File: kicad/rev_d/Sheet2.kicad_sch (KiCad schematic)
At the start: 181 parts, among them J10 vg_old, J5 external clock, J6 JUMPER, J8 JUMPER, J9 JUMPER, Q2 QUARTZ, Q3 QUARTZ32768, U2 PCA9555DB, X11 KEYB-MOUSE, X12 IDC20, X13 USB_C, X15 PLB2-2, X19 AVR pgm conn, X3 IDC26LPT, X4 IDC10M, X5 IDC10M, X6 RS232_9

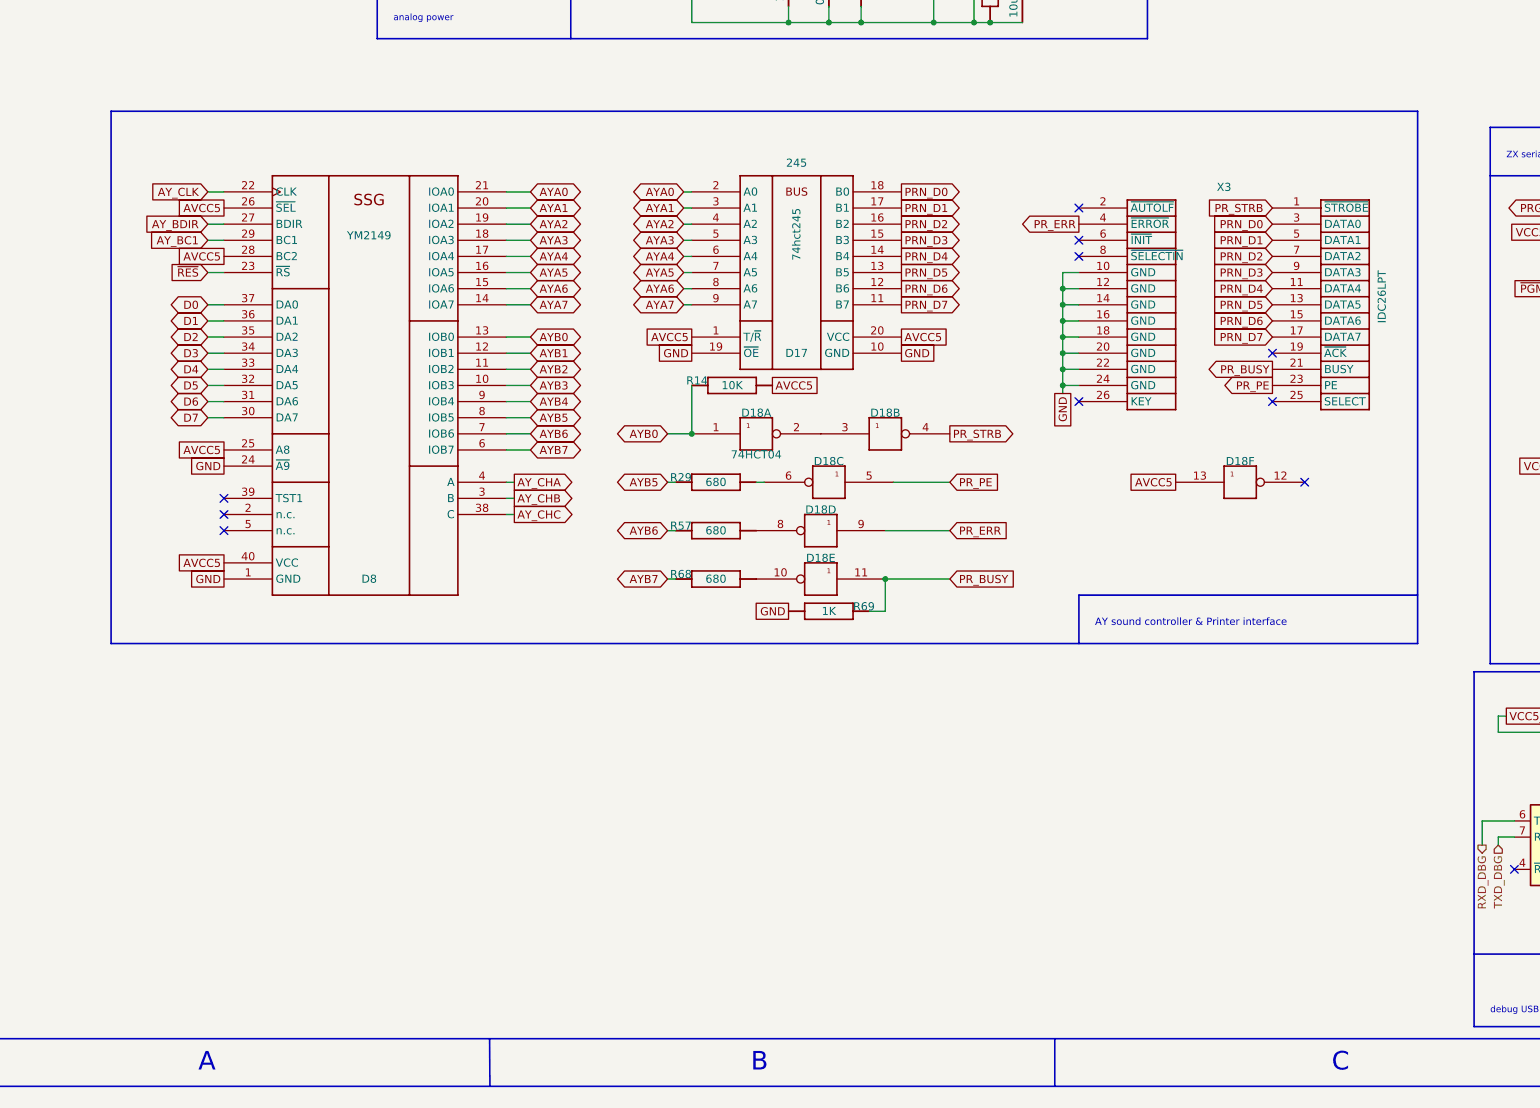
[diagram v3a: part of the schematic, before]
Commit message: pentevo: rev D: add turbosound connector parallel to AY
git-svn-id: svn://localhost/local-pentevo@1264 c6c76956-fad2-4150-a3a9-ea0a427205ba
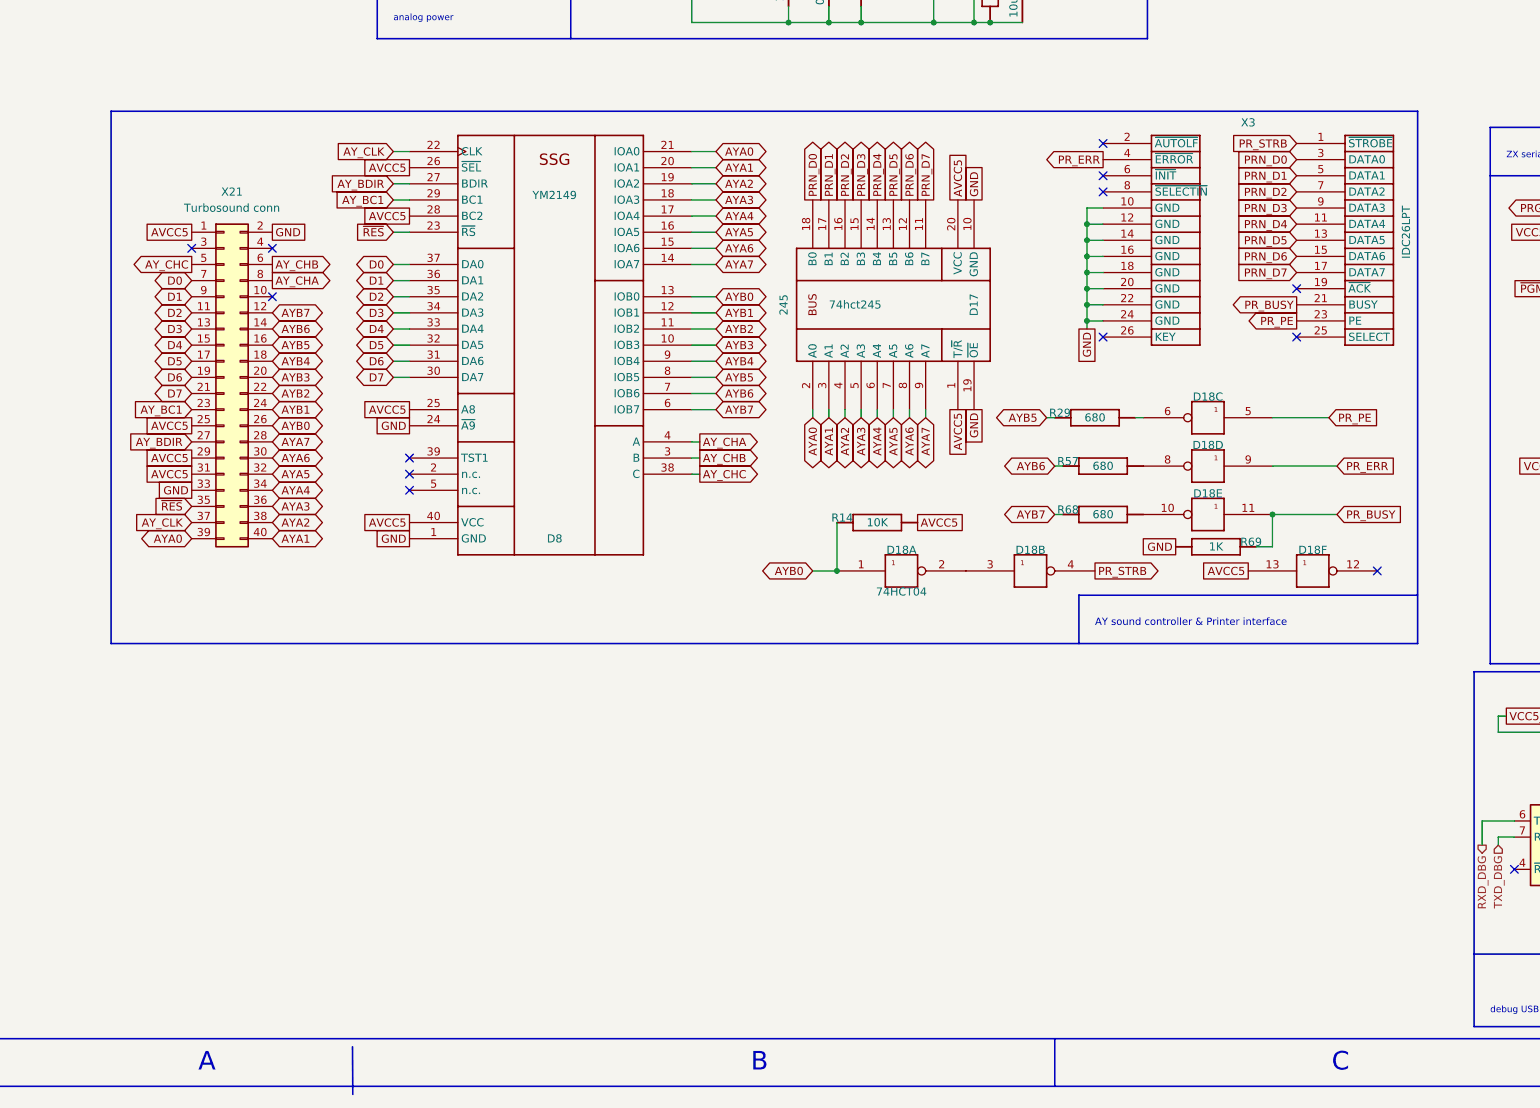
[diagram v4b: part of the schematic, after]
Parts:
- added X21: Turbosound conn, Connector_IDC:IDC-Header_2x20_P2.54mm_Vertical, symbol Connector_Generic:Conn_02x20_Odd_Even
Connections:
- net AVCC5: now also X21.1 (Pin_1), X21.25 (Pin_25), X21.29 (Pin_29), X21.31 (Pin_31)
- net AYA0: now also X21.39 (Pin_39)
- net AYA1: now also X21.40 (Pin_40)
- net AYA2: now also X21.38 (Pin_38)
- net AYA3: now also X21.36 (Pin_36)
- net AYA4: now also X21.34 (Pin_34)
- net AYA5: now also X21.32 (Pin_32)
- net AYA6: now also X21.30 (Pin_30)
- net AYA7: now also X21.28 (Pin_28)
- net AYB0: now also X21.26 (Pin_26)
- net AYB1: now also X21.24 (Pin_24)
- net AYB2: now also X21.22 (Pin_22)
- net AYB3: now also X21.20 (Pin_20)
- net AYB4: now also X21.18 (Pin_18)
- net AYB5: now also X21.16 (Pin_16)
- net AYB6: now also X21.14 (Pin_14)
- net AYB7: now also X21.12 (Pin_12)
- net AY_BC1: now also X21.23 (Pin_23)
- net AY_BDIR: now also X21.27 (Pin_27)
- net AY_CHA: now also X21.8 (Pin_8)
- net AY_CHB: now also X21.6 (Pin_6)
- net AY_CHC: now also X21.5 (Pin_5)
- net AY_CLK: now also X21.37 (Pin_37)
- net D0: now also X21.7 (Pin_7)
- net D1: now also X21.9 (Pin_9)
- net D2: now also X21.11 (Pin_11)
- net D3: now also X21.13 (Pin_13)
- net D4: now also X21.15 (Pin_15)
- net D5: now also X21.17 (Pin_17)
- net D6: now also X21.19 (Pin_19)
- net D7: now also X21.21 (Pin_21)
- net GND: now also X21.2 (Pin_2), X21.33 (Pin_33); no longer D18.6, R29.1 (i/o)
- net ~{RES}: now also X21.35 (Pin_35)
- new net: D18.6, R29.1 (i/o)
- no-connect marks 33 -> 36
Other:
- moved on the sheet: D17, D18A, D18B, D18C, D18D, D18E, D18F, D8, R14, R29, R57, R68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

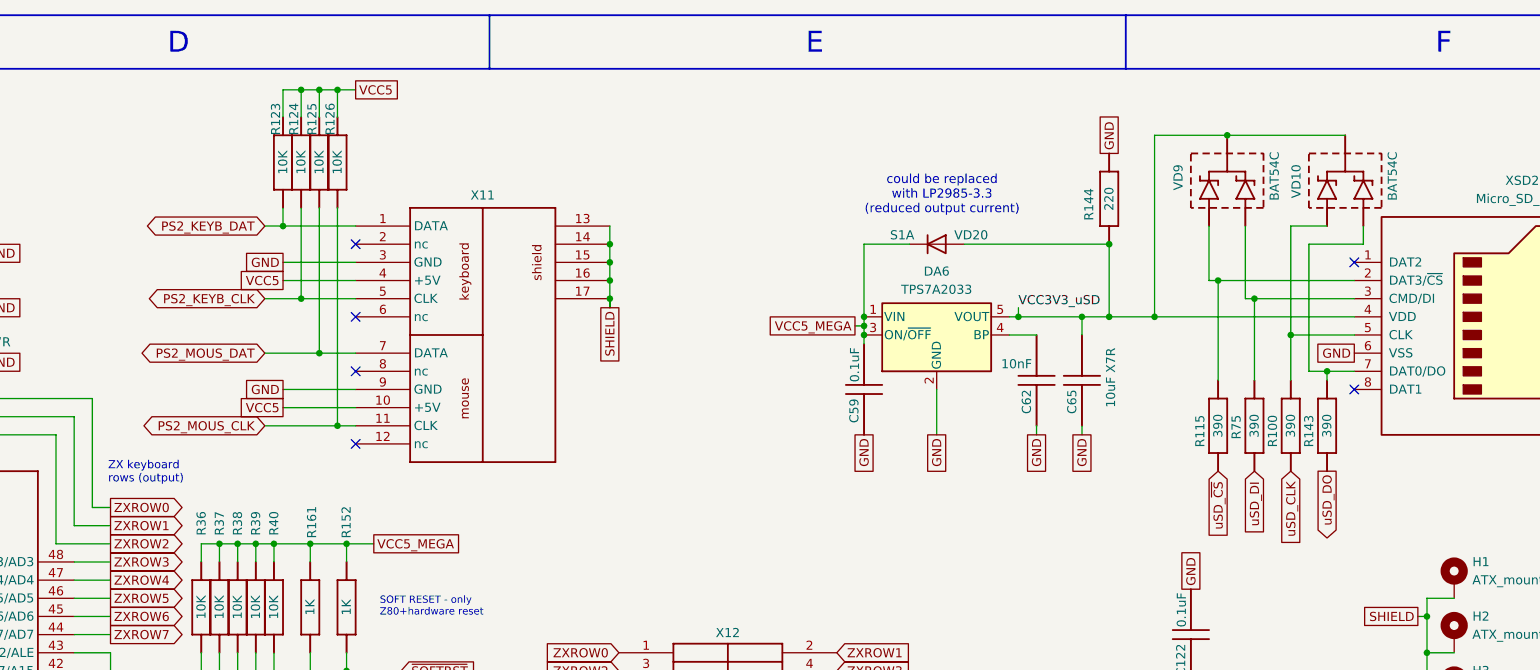
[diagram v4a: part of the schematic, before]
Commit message: pentevo: rev D: add extra PS2 connector for extenders (like USB-PS2)
git-svn-id: svn://localhost/local-pentevo@1265 c6c76956-fad2-4150-a3a9-ea0a427205ba
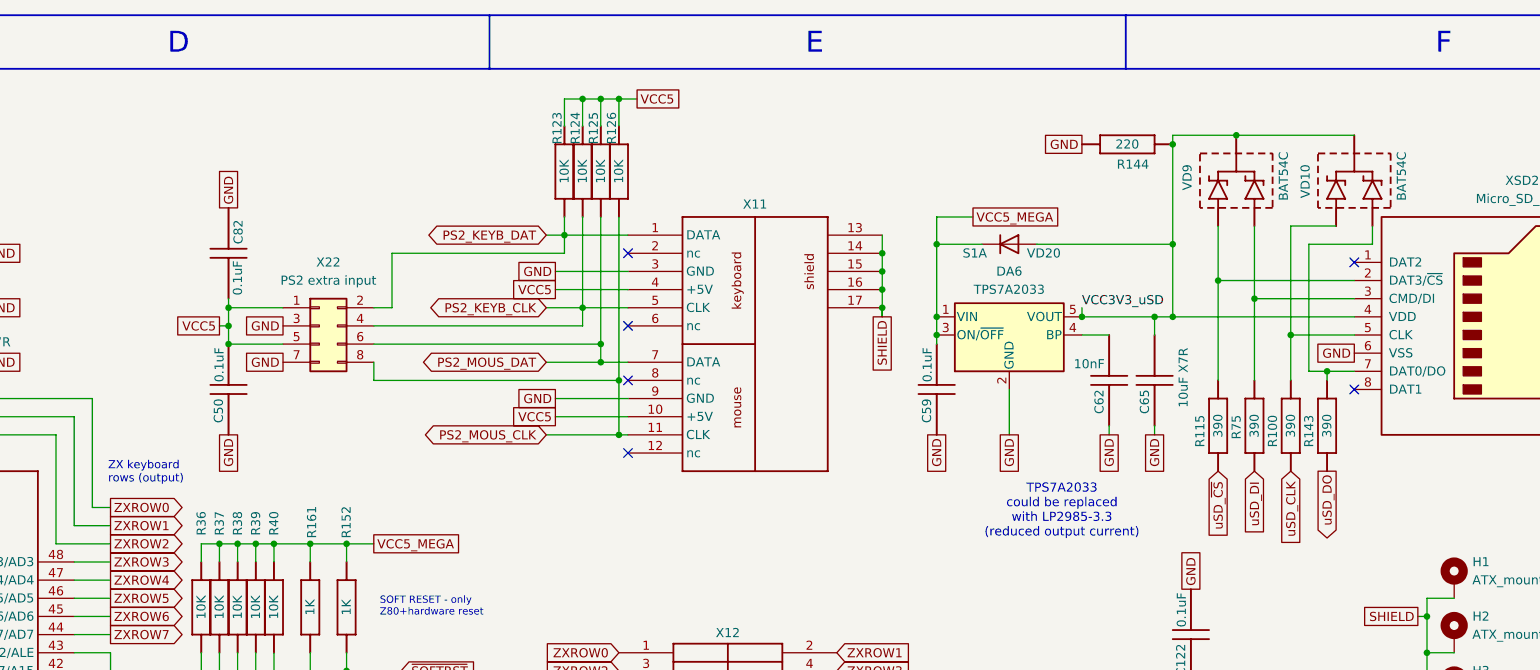
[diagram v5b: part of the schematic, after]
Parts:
- added C50, C82: 0.1uF, C-CHIP, symbol eva-altium-import:Sheet2_0_CAPCHIP
- added X22: PS2 extra input, Connector_PinSocket_2.54mm:PinSocket_2x04_P2.54mm_Vertical, symbol Connector_Generic:Conn_02x04_Odd_Even
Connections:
- net GND: now also C50.1, C82.1, X22.3 (Pin_3), X22.7 (Pin_7)
- net PS2_KEYB_CLK: now also X22.4 (Pin_4)
- net PS2_KEYB_DAT: now also X22.2 (Pin_2)
- net PS2_MOUS_CLK: now also X22.8 (Pin_8)
- net PS2_MOUS_DAT: now also X22.6 (Pin_6)
- net VCC5: now also C50.2, C82.2, X22.1 (Pin_1), X22.5 (Pin_5)
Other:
- note added: "TPS7A2033 could be replaced with LP2985-3.3 (reduced output current)"
- note removed: "could be replaced with LP2985-3.3 (reduced output current)"
- moved on the sheet: C59, C62, C65, DA6, R123, R124, R125, R126, R144, VD10, VD20, VD9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

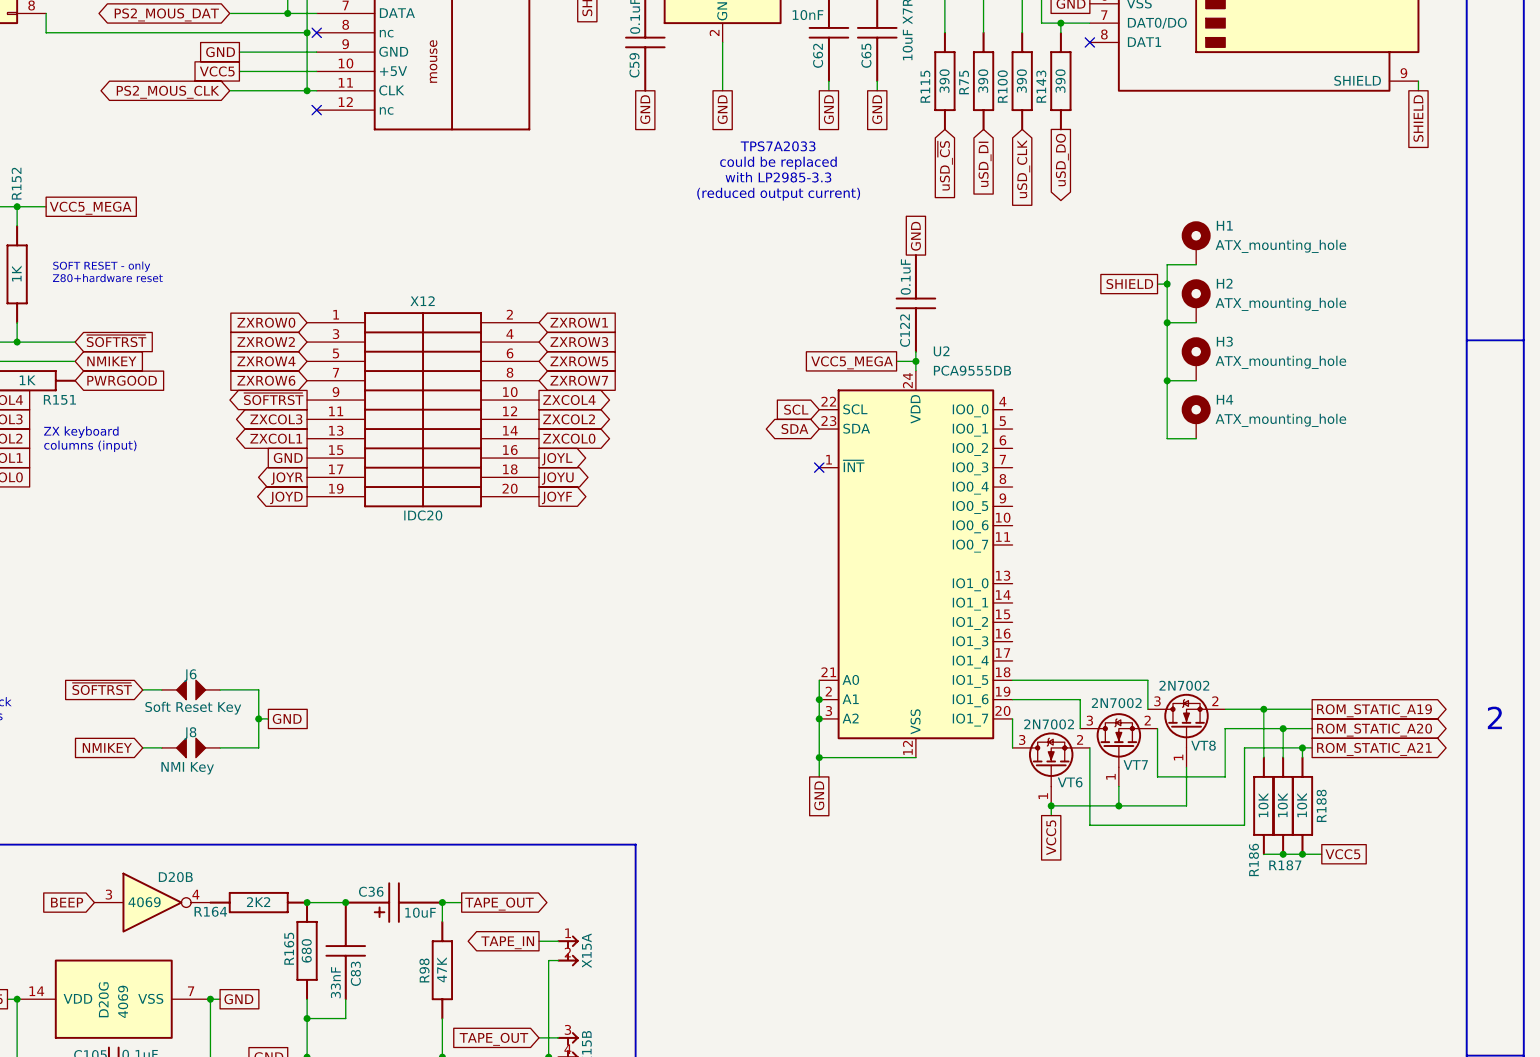
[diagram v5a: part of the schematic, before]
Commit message: pentevo: rev D: add 2x SEGA pads through pca9555
git-svn-id: svn://localhost/local-pentevo@1267 c6c76956-fad2-4150-a3a9-ea0a427205ba
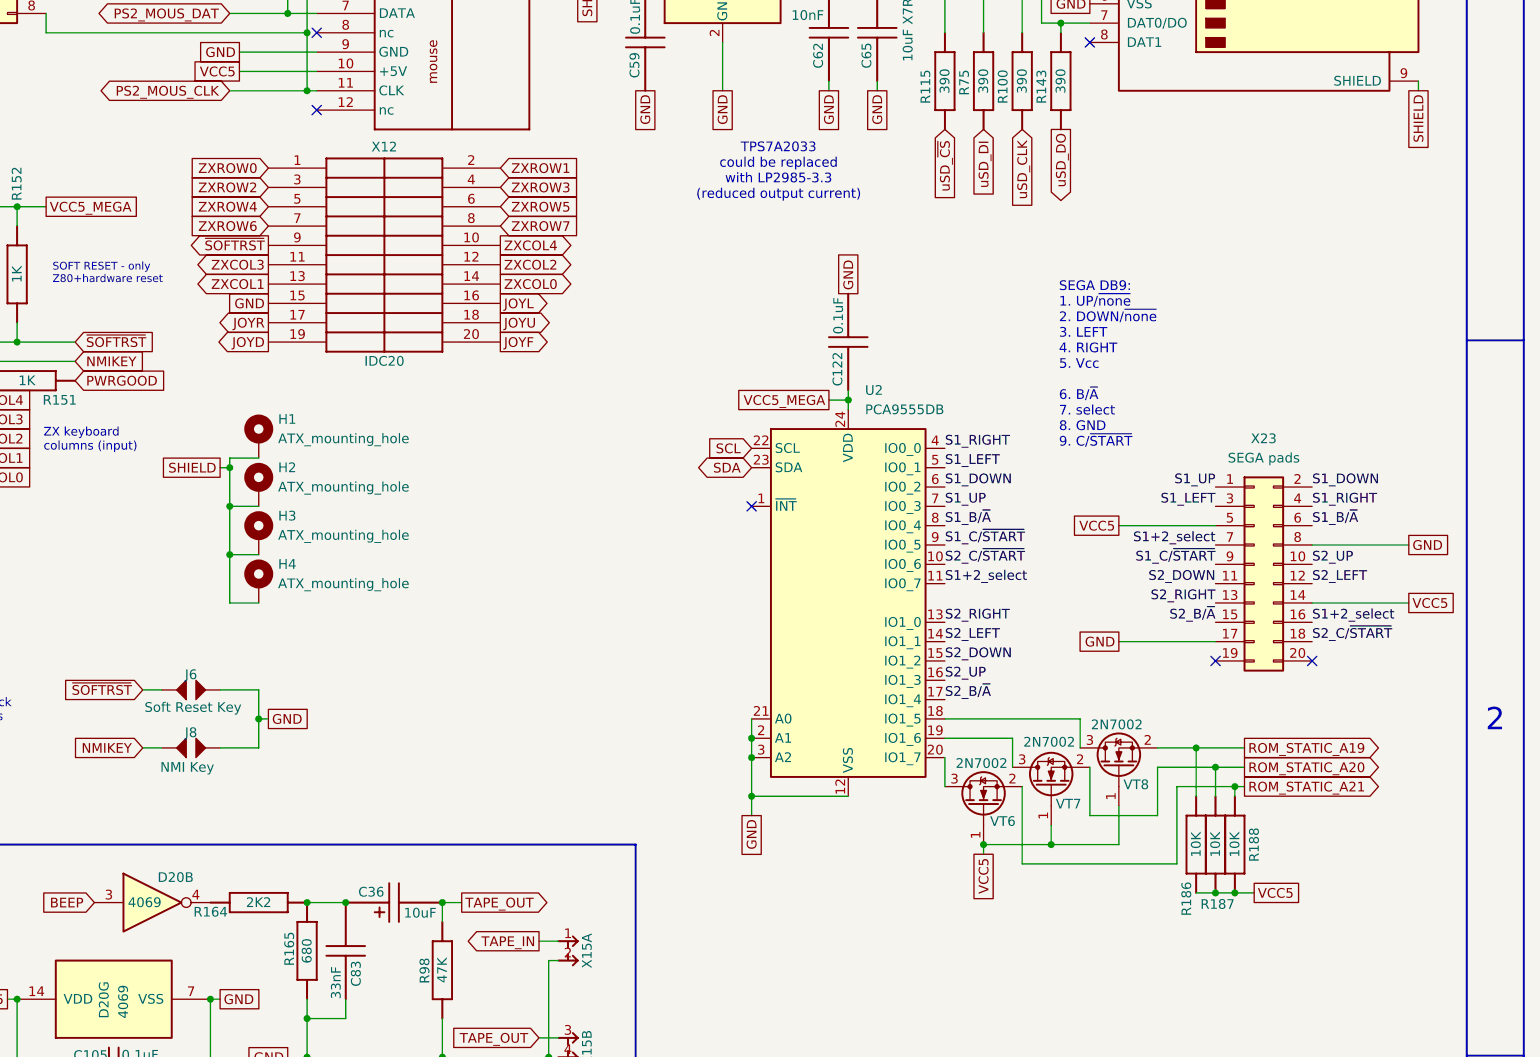
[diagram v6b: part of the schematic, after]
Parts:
- added X23: SEGA pads, symbol Connector_Generic:Conn_02x10_Odd_Even
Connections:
- net GND: now also X23.17 (Pin_17), X23.8 (Pin_8)
- net VCC5: now also X23.14 (Pin_14), X23.5 (Pin_5)
- net S2_C/~{START}: now reaches U2.10 (IO0_6)
- net S2_C/~{START}: now also X23.18 (Pin_18)
- net S1+2_select: now reaches U2.11 (IO0_7)
- net S1+2_select: now also X23.16 (Pin_16), X23.7 (Pin_7)
- net S2_RIGHT: now reaches U2.13 (IO1_0)
- net S2_RIGHT: now also X23.13 (Pin_13)
- net S2_LEFT: now reaches U2.14 (IO1_1)
- net S2_LEFT: now also X23.12 (Pin_12)
- net S2_DOWN: now reaches U2.15 (IO1_2)
- net S2_DOWN: now also X23.11 (Pin_11)
- net S2_UP: now reaches U2.16 (IO1_3)
- net S2_UP: now also X23.10 (Pin_10)
- net S2_B/~{A}: now reaches U2.17 (IO1_4)
- net S2_B/~{A}: now also X23.15 (Pin_15)
- net S1_RIGHT: now reaches U2.4 (IO0_0)
- net S1_RIGHT: now also X23.4 (Pin_4)
- net S1_LEFT: now reaches U2.5 (IO0_1)
- net S1_LEFT: now also X23.3 (Pin_3)
- net S1_DOWN: now reaches U2.6 (IO0_2)
- net S1_DOWN: now also X23.2 (Pin_2)
- net S1_UP: now reaches U2.7 (IO0_3)
- net S1_UP: now also X23.1 (Pin_1)
- net S1_B/~{A}: now reaches U2.8 (IO0_4)
- net S1_B/~{A}: now also X23.6 (Pin_6)
- net S1_C/~{START}: now reaches U2.9 (IO0_5)
- net S1_C/~{START}: now also X23.9 (Pin_9)
- no-connect marks 36 -> 38
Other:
- note added: "SEGA DB9: 1. UP/~{none} 2. DOWN/~{none} 3. LEFT 4. RIGHT 5. Vcc 6. B/~{A} 7. select 8. GND 9. C/~{START}"
- moved on the sheet: C122, H1, H2, H3, H4, R186, R187, R188, U2, VT6, VT7, VT8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
